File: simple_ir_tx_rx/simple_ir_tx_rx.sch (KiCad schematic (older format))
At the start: 14 parts, among them J1 CONN_01X05, Q1 Q_NMOS_GSD, Q2 Q_PMOS_GSD, U1 TSOP45xx

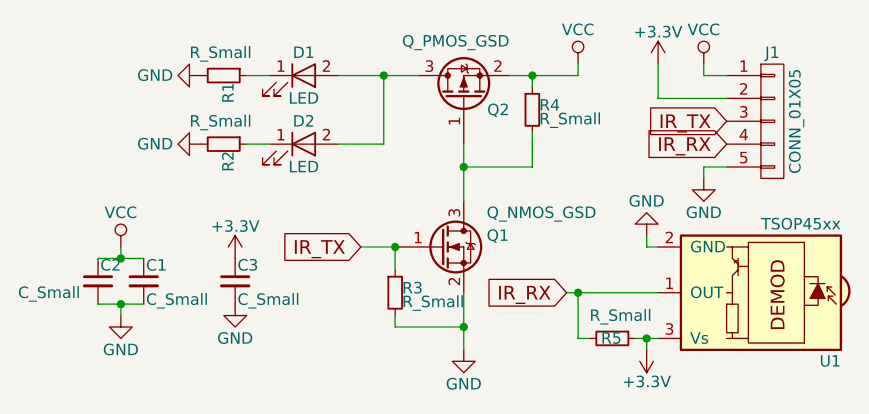
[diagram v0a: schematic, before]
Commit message: Added version information, updated pinout
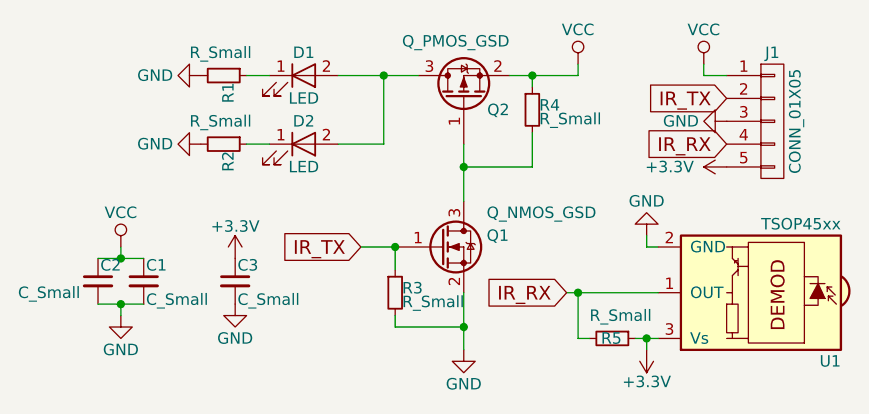
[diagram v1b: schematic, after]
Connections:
- net +3V3: now also J1.5 (P5); no longer J1.2 (P2)
- net GND: now also J1.3 (P3); no longer J1.5 (P5)
- net IR_TX: now also J1.2 (P2); no longer J1.3 (P3)
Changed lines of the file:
@@
 LIBS:contrib
 LIBS:valves
-LIBS:tsop4838
 LIBS:simple_ir_tx_rx-cache
 EELAYER 25 0
@@
 L +3.3V #PWR11
 U 1 1 5992EF72
-P 6800 2850
-F 0 "#PWR11" H 6800 2700 50  0001 C CNN
-F 1 "+3.3V" H 6800 2990 50  0000 C CNN
-F 2 "" H 6800 2850 50  0001 C CNN
-F 3 "" H 6800 2850 50  0001 C CNN
-	1    6800 2850
-	1    0    0    -1
+P 7100 3300
+F 0 "#PWR11" H 7100 3150 50  0001 C CNN
+F 1 "+3.3V" V 7100 3550 50  0000 C CNN
+F 2 "" H 7100 3300 50  0001 C CNN
+F 3 "" H 7100 3300 50  0001 C CNN
+	1    7100 3300
+	0    -1   -1   0
 $EndComp
 $Comp
@@
 L GND #PWR13
 U 1 1 5992EFC5
-P 7000 3350
-F 0 "#PWR13" H 7000 3100 50  0001 C CNN
-F 1 "GND" H 7000 3200 50  0000 C CNN
-F 2 "" H 7000 3350 50  0001 C CNN
-F 3 "" H 7000 3350 50  0001 C CNN
-	1    7000 3350
-	1    0    0    -1
+P 7100 3100
+F 0 "#PWR13" H 7100 2850 50  0001 C CNN
+F 1 "GND" V 7100 2900 50  0000 C CNN
+F 2 "" H 7100 3100 50  0001 C CNN
+F 3 "" H 7100 3100 50  0001 C CNN
+	1    7100 3100
+	0    1    1    0
 $EndComp
 Wire Wire Line
@@
 	7000 2900 7100 2900
 Wire Wire Line
-	7100 3000 6800 3000
-Wire Wire Line
-	6800 3000 6800 2850
-Wire Wire Line
-	7100 3300 7000 3300
-Wire Wire Line
-	7000 3300 7000 3350
-Wire Wire Line
 	6450 2900 6450 2850
 Connection ~ 6250 2900
@@
 IR_TX
 Connection ~ 5650 3650
-Text GLabel 7100 3100 0    60   Input ~ 0
+Text GLabel 7100 3000 0    60   Input ~ 0
 IR_TX
 $Comp
